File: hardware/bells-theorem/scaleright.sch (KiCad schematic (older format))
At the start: 17 parts, among them U19 TL074

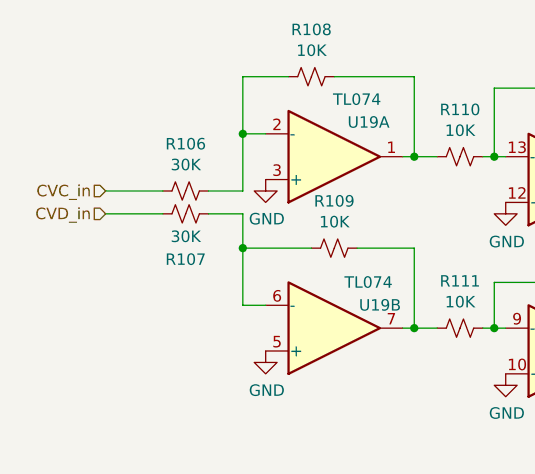
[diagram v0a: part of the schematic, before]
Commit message: take gerbers out of the repo, push latest updates
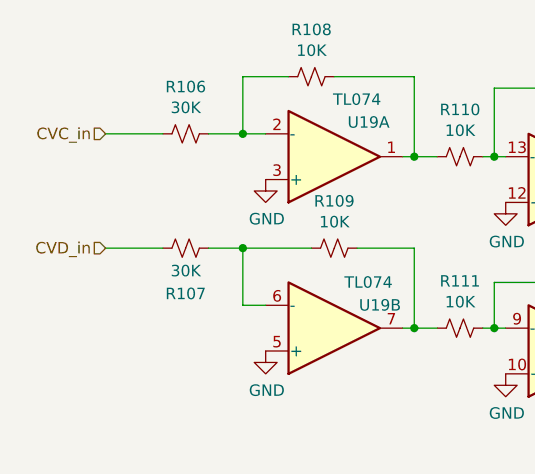
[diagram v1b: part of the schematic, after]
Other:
- moved on the sheet: R106, R107
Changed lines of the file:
@@
 $Descr A4 11693 8268
 encoding utf-8
-Sheet 7 8
+Sheet 8 8
 Title ""
 Date ""
@@
 L device:R_Small_US R?
 U 1 1 5F8A66B2
-P 3450 2350
+P 3450 2100
 AR Path="/5CEF66AD/5F9DE87B/5F8A66B2" Ref="R?"  Part="1"
 AR Path="/5CEF66AD/5F8906B5/5F8A66B2" Ref="R106"  Part="1"
-F 0 "R106" V 3245 2350 50  0000 C CNN
-F 1 "30K" V 3336 2350 50  0000 C CNN
-F 2 "Resistor_SMD:R_0805_2012Metric_Pad1.15x1.40mm_HandSolder" H 3450 2350 50  0001 C CNN
-F 3 "~" H 3450 2350 50  0001 C CNN
-	1    3450 2350
+F 0 "R106" V 3245 2100 50  0000 C CNN
+F 1 "30K" V 3336 2100 50  0000 C CNN
+F 2 "Resistor_SMD:R_0805_2012Metric_Pad1.15x1.40mm_HandSolder" H 3450 2100 50  0001 C CNN
+F 3 "~" H 3450 2100 50  0001 C CNN
+	1    3450 2100
 	0    1    1    0
 $EndComp
@@
 L device:R_Small_US R?
 U 1 1 5F8A66B8
-P 3450 2450
+P 3450 2600
 AR Path="/5CEF66AD/5F9DE87B/5F8A66B8" Ref="R?"  Part="1"
 AR Path="/5CEF66AD/5F8906B5/5F8A66B8" Ref="R107"  Part="1"
-F 0 "R107" V 3650 2450 50  0000 C CNN
-F 1 "30K" V 3550 2450 50  0000 C CNN
-F 2 "Resistor_SMD:R_0805_2012Metric_Pad1.15x1.40mm_HandSolder" H 3450 2450 50  0001 C CNN
-F 3 "~" H 3450 2450 50  0001 C CNN
-	1    3450 2450
+F 0 "R107" V 3650 2600 50  0000 C CNN
+F 1 "30K" V 3550 2600 50  0000 C CNN
+F 2 "Resistor_SMD:R_0805_2012Metric_Pad1.15x1.40mm_HandSolder" H 3450 2600 50  0001 C CNN
+F 3 "~" H 3450 2600 50  0001 C CNN
+	1    3450 2600
 	0    1    1    0
 $EndComp
@@
 $EndComp
 Wire Wire Line
-	3550 2350 3700 2350
-Wire Wire Line
-	3700 2350 3700 2100
+	3550 2100 3700 2100
 Wire Wire Line
 	3700 2100 3800 2100
@@
 	4800 2200 4850 2200
 Wire Wire Line
-	3550 2450 3700 2450
-Wire Wire Line
-	3700 2450 3700 2600
+	3550 2600 3700 2600
 Wire Wire Line
 	3700 2850 3800 2850
@@
 	6700 3050 6950 3050
 Wire Wire Line
-	3350 2350 3100 2350
-Wire Wire Line
-	3350 2450 3100 2450
-Text HLabel 3100 2350 0    50   Input ~ 0
+	3350 2100 3100 2100
+Wire Wire Line
+	3350 2600 3100 2600
+Text HLabel 3100 2100 0    50   Input ~ 0
 CVC_in
-Text HLabel 3100 2450 0    50   Input ~ 0
+Text HLabel 3100 2600 0    50   Input ~ 0
 CVD_in
 $Comp

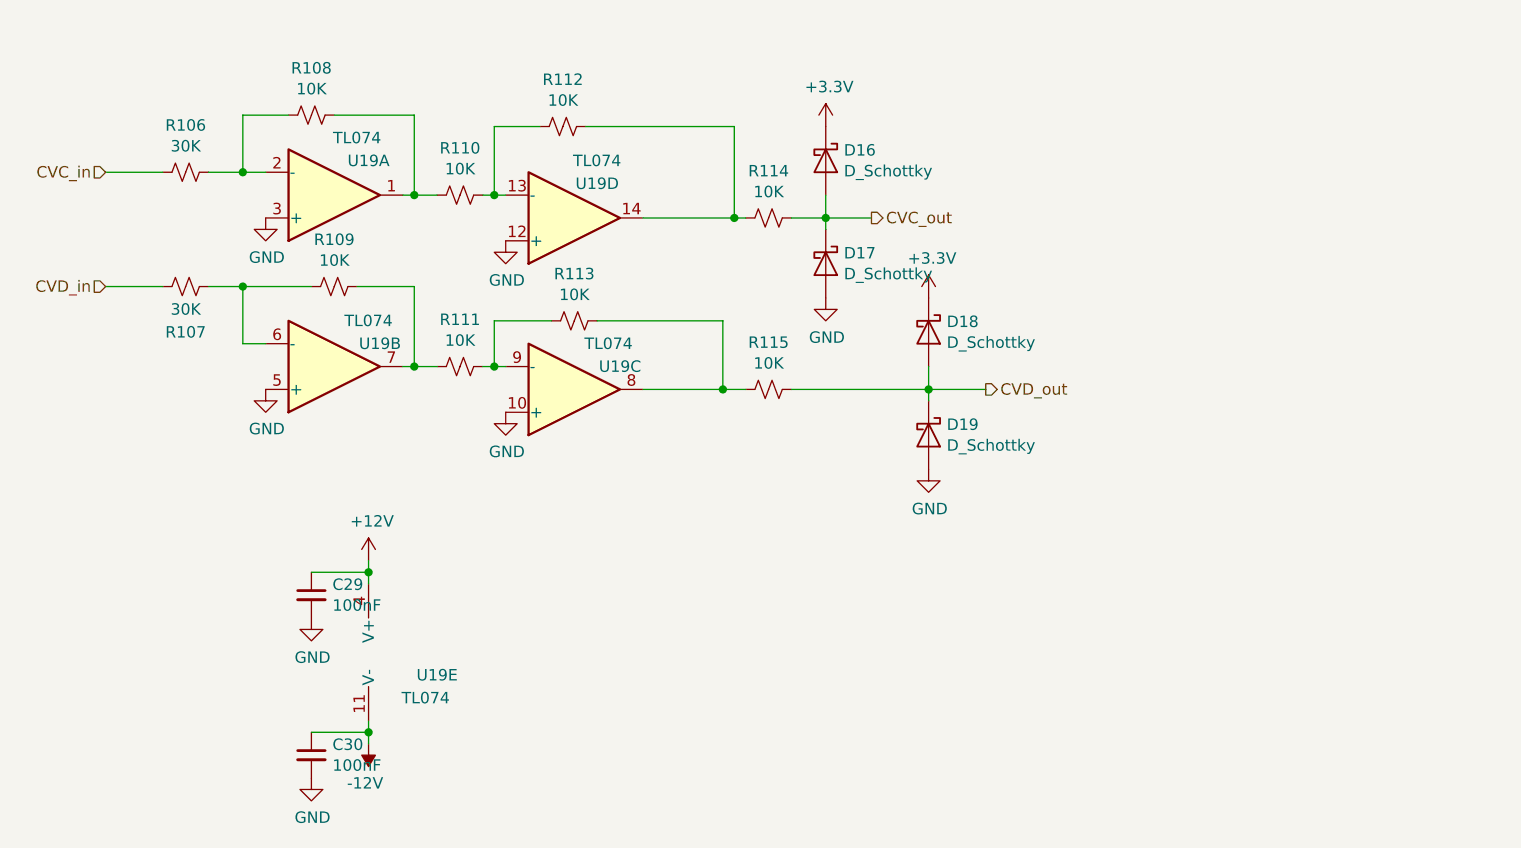
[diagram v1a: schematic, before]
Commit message: modified for Kicad 6 updated testing code
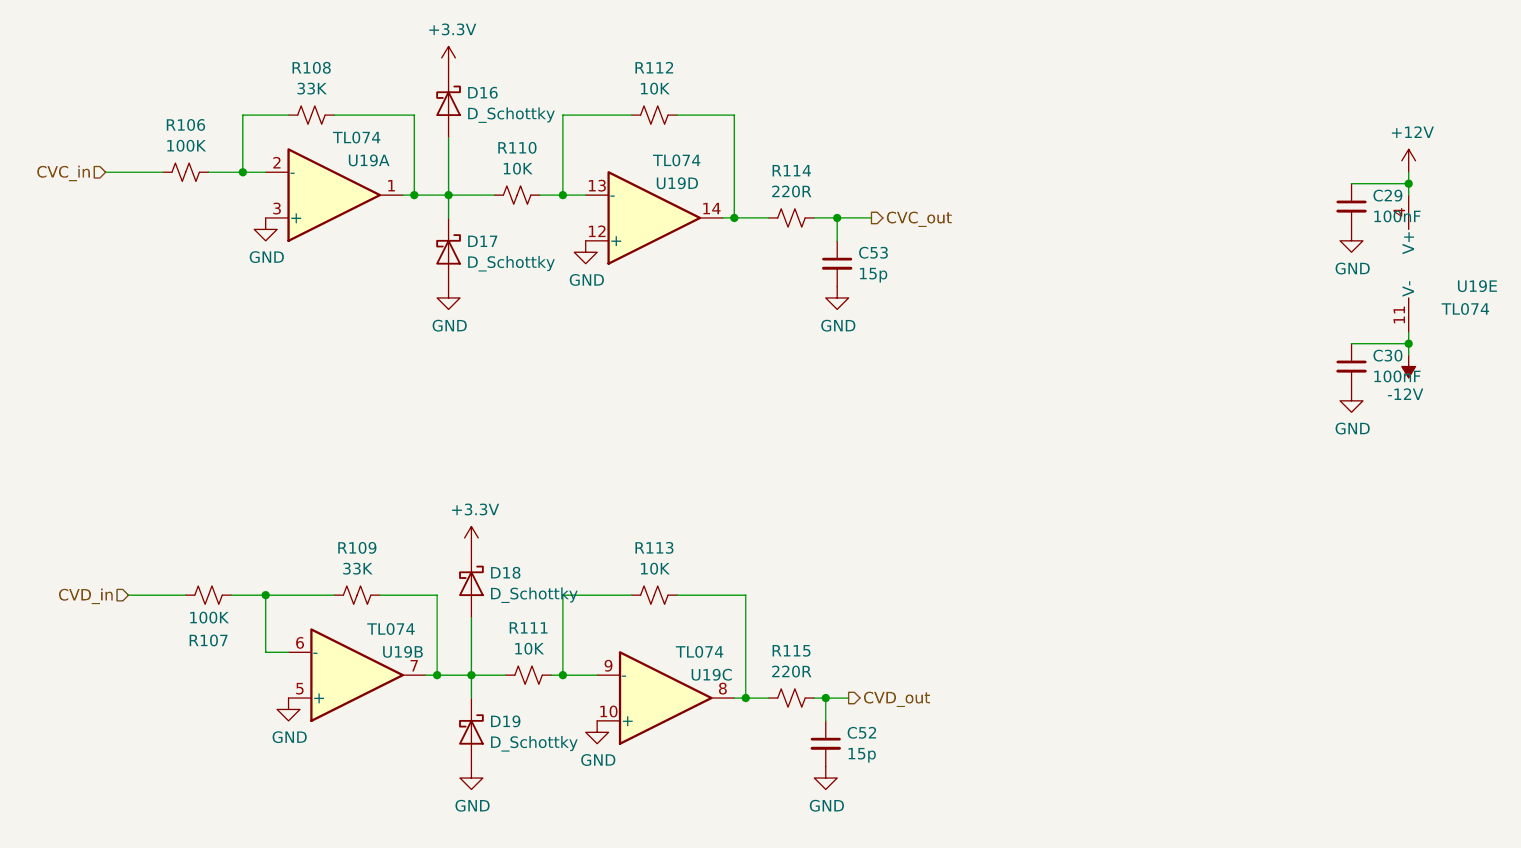
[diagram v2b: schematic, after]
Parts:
- added C52, C53: 15p, symbol device:C_Small
- R106, R107: value 30K -> 100K
- R108, R109: value 10K -> 33K
- R114, R115: value 10K -> 220R
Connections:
- net CVC_out: now also C53.1; no longer D16.2 (A), D17.1 (K)
- net CVD_out: now also C52.1; no longer D18.2 (A), D19.1 (K)
- net GND: now also C52.2, C53.2
- net at R108.1, R110.2, U19.1: now also D16.2 (A), D17.1 (K)
- net at R109.1, R111.2, U19.7: now also D18.2 (A), D19.1 (K)
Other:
- moved on the sheet: C29, C30, D16, D17, D18, D19, R107, R109, R110, R111, R112, R113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
